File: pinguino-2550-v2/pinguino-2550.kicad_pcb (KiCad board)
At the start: 2 copper layers, 100 x 50 mm, 28 parts, among them J1 USB, J10 D1, J11 D2, J12 D3, J2 BATT, J3 SELECT, J4 A0, J5 A1, J6 PWM-1, J8 UART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

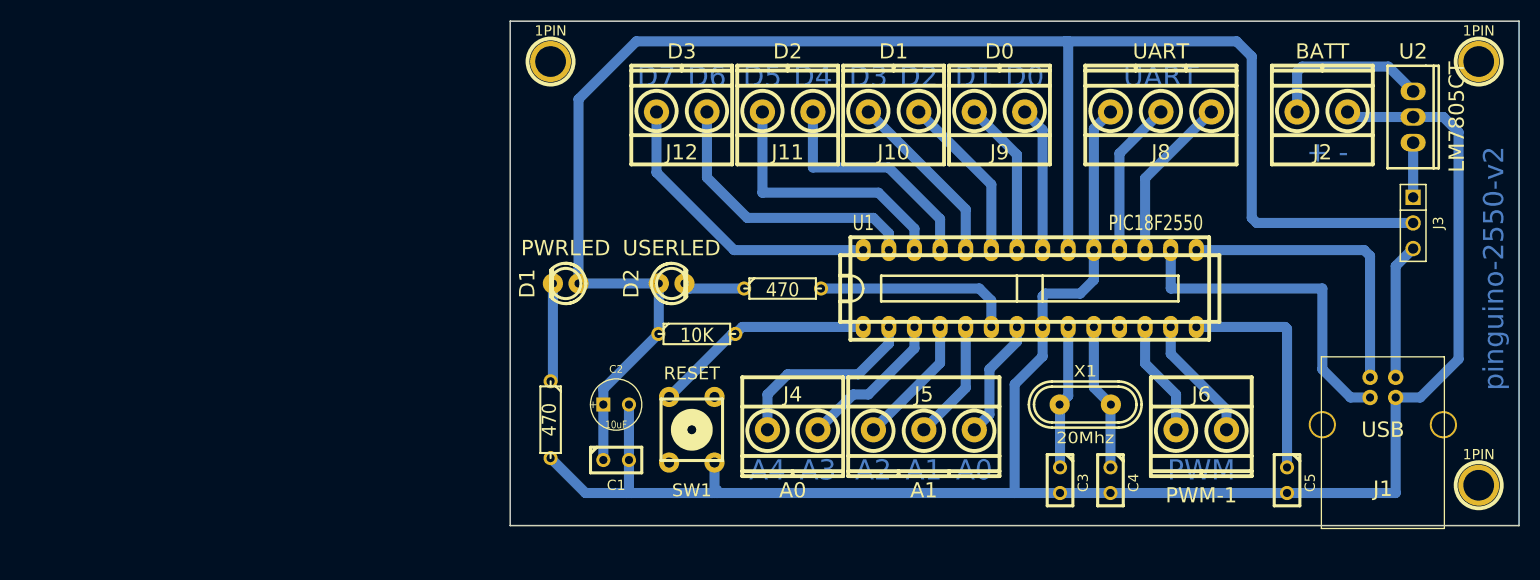
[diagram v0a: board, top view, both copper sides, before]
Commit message: Added BoM. Fixed pcbnew paper size.
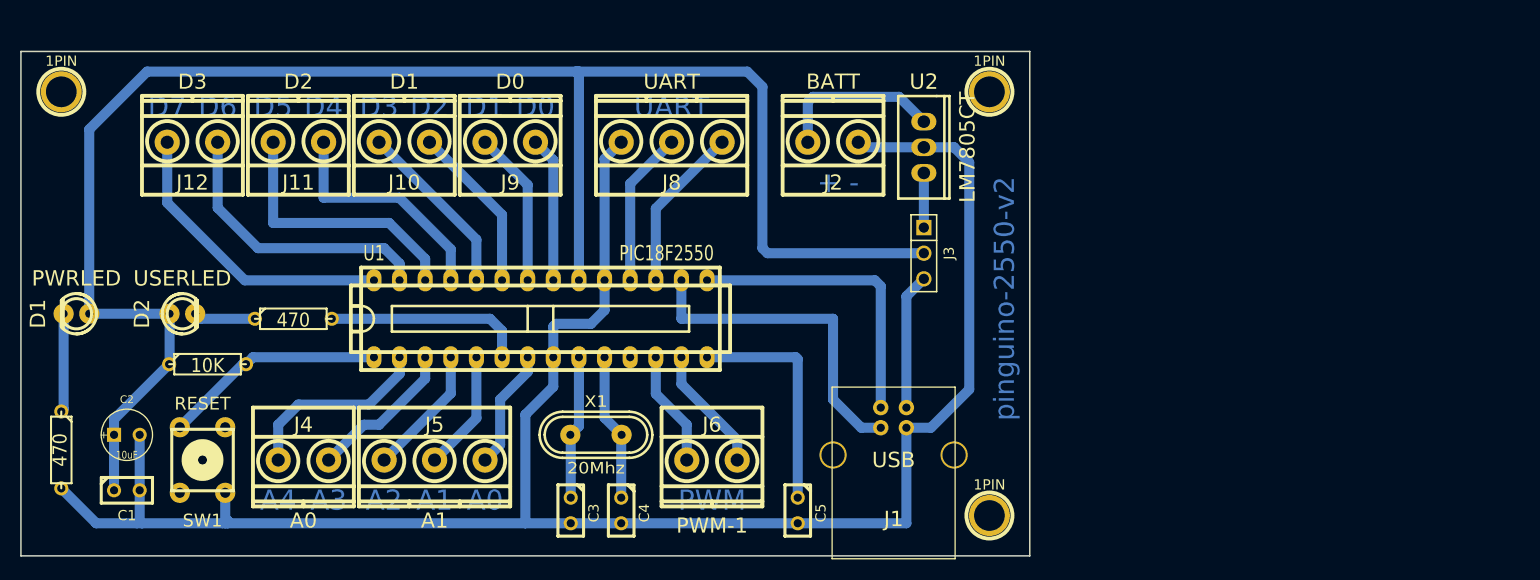
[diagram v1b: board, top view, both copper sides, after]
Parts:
- moved 1PIN 48.6 mm to (147.5, 90.0)
- moved 1PIN 48.6 mm to (147.5, 48.0)
- moved 1PIN 48.6 mm to (55.5, 48.0)
- moved C1 48.6 mm to (62.0, 87.5)
- moved C2 48.6 mm to (62.0, 82.0)
- moved C3 48.6 mm to (106.0, 89.5)
- moved C4 48.6 mm to (111.0, 89.5)
- moved C5 48.6 mm to (128.5, 89.5)
- moved D1 48.6 mm to (57.0, 70.0)
- moved D2 48.6 mm to (67.5, 70.0)
- moved J1 48.6 mm to (138.0, 84.0)
- moved J10 48.6 mm to (89.5, 53.0)
- moved J11 48.6 mm to (79.0, 53.0)
- moved J12 48.6 mm to (68.5, 53.0)
- moved J2 48.6 mm to (132.0, 53.0)
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
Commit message: Cupper layer text mirroring.
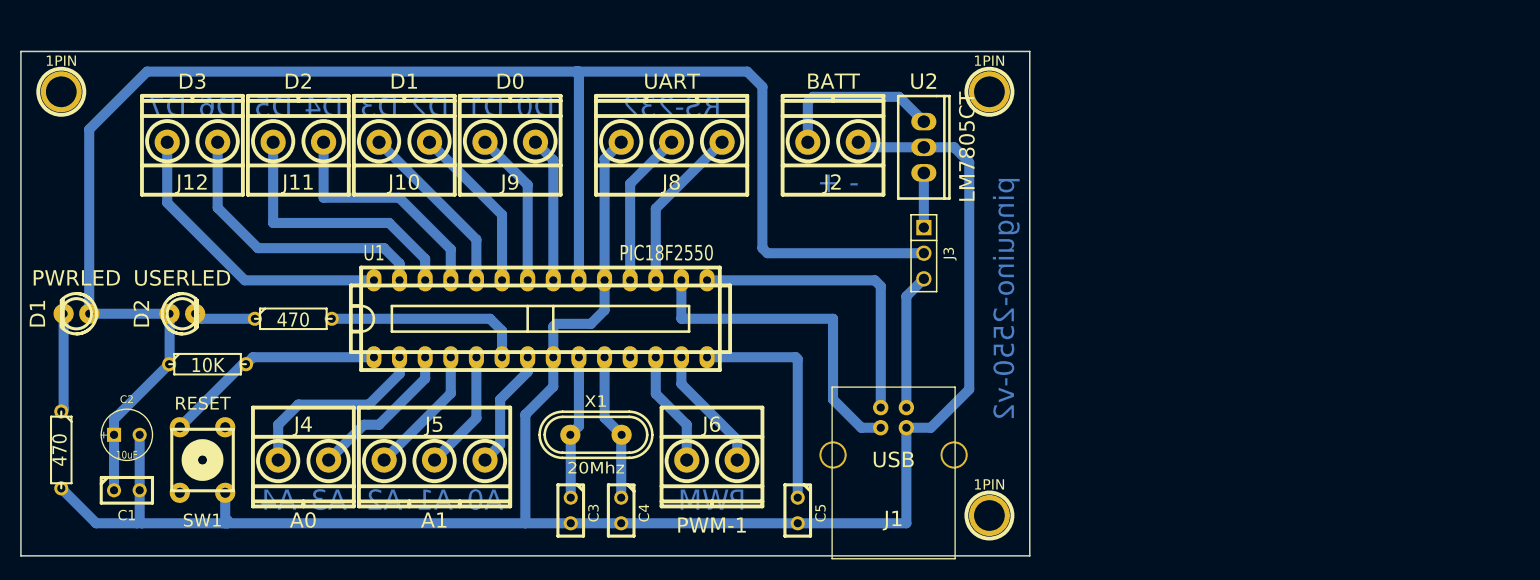
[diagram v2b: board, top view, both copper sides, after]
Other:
- board text added: "RS-232"
- board text removed: "UART"
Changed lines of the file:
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@@
     (links 50)
     (no_connects 0)
-    (area 23.85 31.925001 214.577381 413.25)
+    (area 13.35 34.925001 166.077381 283.35)
     (thickness 1.6)
     (drawings 24)
@@
     (nets 32)
   )
-  (page User 210.007 297.002 portrait)
+  (page User 431.8 279.4 portrait)
   (title_block
     (title "Pinguino 2550")
@@
     (19 F.Paste user hide)
     (20 B.SilkS user hide)
-    (21 F.SilkS user hide)
+    (21 F.SilkS user)
     (22 B.Mask user hide)
     (23 F.Mask user hide)
@@
   )
   (gr_text A4 (at 77 88.5) (layer B.Cu)
-    (effects (font (size 2 2) (thickness 0.3)))
+    (effects (font (size 2 2) (thickness 0.3)) (justify mirror))
   )
   (gr_text A3 (at 82 88.5) (layer B.Cu)
-    (effects (font (size 2 2) (thickness 0.3)))
+    (effects (font (size 2 2) (thickness 0.3)) (justify mirror))
   )
   (gr_text A2 (at 87.5 88.5) (layer B.Cu)
-    (effects (font (size 2 2) (thickness 0.3)))
+    (effects (font (size 2 2) (thickness 0.3)) (justify mirror))
   )
   (gr_text A1 (at 92.5 88.5) (layer B.Cu)
-    (effects (font (size 2 2) (thickness 0.3)))
+    (effects (font (size 2 2) (thickness 0.3)) (justify mirror))
   )
   (gr_text A0 (at 97.5 88.5) (layer B.Cu)
-    (effects (font (size 2 2) (thickness 0.3)))
+    (effects (font (size 2 2) (thickness 0.3)) (justify mirror))
   )
   (gr_text PWM (at 120 88.5) (layer B.Cu)
-    (effects (font (size 2 2) (thickness 0.3)))
+    (effects (font (size 2 2) (thickness 0.3)) (justify mirror))
   )
   (gr_text D7 (at 66 49.5) (layer B.Cu)
-    (effects (font (size 2 2) (thickness 0.3)))
+    (effects (font (size 2 2) (thickness 0.3)) (justify mirror))
   )
   (gr_text D6 (at 71 49.5) (layer B.Cu)
-    (effects (font (size 2 2) (thickness 0.3)))
+    (effects (font (size 2 2) (thickness 0.3)) (justify mirror))
   )
   (gr_text D5 (at 76.5 49.5) (layer B.Cu)
-    (effects (font (size 2 2) (thickness 0.3)))
+    (effects (font (size 2 2) (thickness 0.3)) (justify mirror))
   )
   (gr_text D4 (at 81.5 49.5) (layer B.Cu)
-    (effects (font (size 2 2) (thickness 0.3)))
+    (effects (font (size 2 2) (thickness 0.3)) (justify mirror))
   )
   (gr_text D3 (at 87 49.5) (layer B.Cu)
-    (effects (font (size 2 2) (thickness 0.3)))
+    (effects (font (size 2 2) (thickness 0.3)) (justify mirror))
   )
   (gr_text D2 (at 92 49.5) (layer B.Cu)
-    (effects (font (size 2 2) (thickness 0.3)))
+    (effects (font (size 2 2) (thickness 0.3)) (justify mirror))
   )
   (gr_text D1 (at 97.5 49.5) (layer B.Cu)
-    (effects (font (size 2 2) (thickness 0.3)))
+    (effects (font (size 2 2) (thickness 0.3)) (justify mirror))
   )
   (gr_text D0 (at 102.5 49.5) (layer B.Cu)
-    (effects (font (size 2 2) (thickness 0.3)))
-  )
-  (gr_text UART (at 116 49.5) (layer B.Cu)
-    (effects (font (size 2 2) (thickness 0.3)))
+    (effects (font (size 2 2) (thickness 0.3)) (justify mirror))
+  )
+  (gr_text RS-232 (at 116 49.5) (layer B.Cu)
+    (effects (font (size 2 2) (thickness 0.3)) (justify mirror))
   )
   (gr_text "+ -" (at 132.5 57) (layer B.Cu)
@@
   )
   (gr_text pinguino-2550-v2 (at 149 68.5 90) (layer B.Cu)
-    (effects (font (size 2 2) (thickness 0.3)))
+    (effects (font (size 2 2) (thickness 0.3)) (justify mirror))
   )
   (gr_line (start 51.5 44) (end 151.5 44) (angle 90) (layer Edge.Cuts) (width 0.15))

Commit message: Fixed bornier modules text.
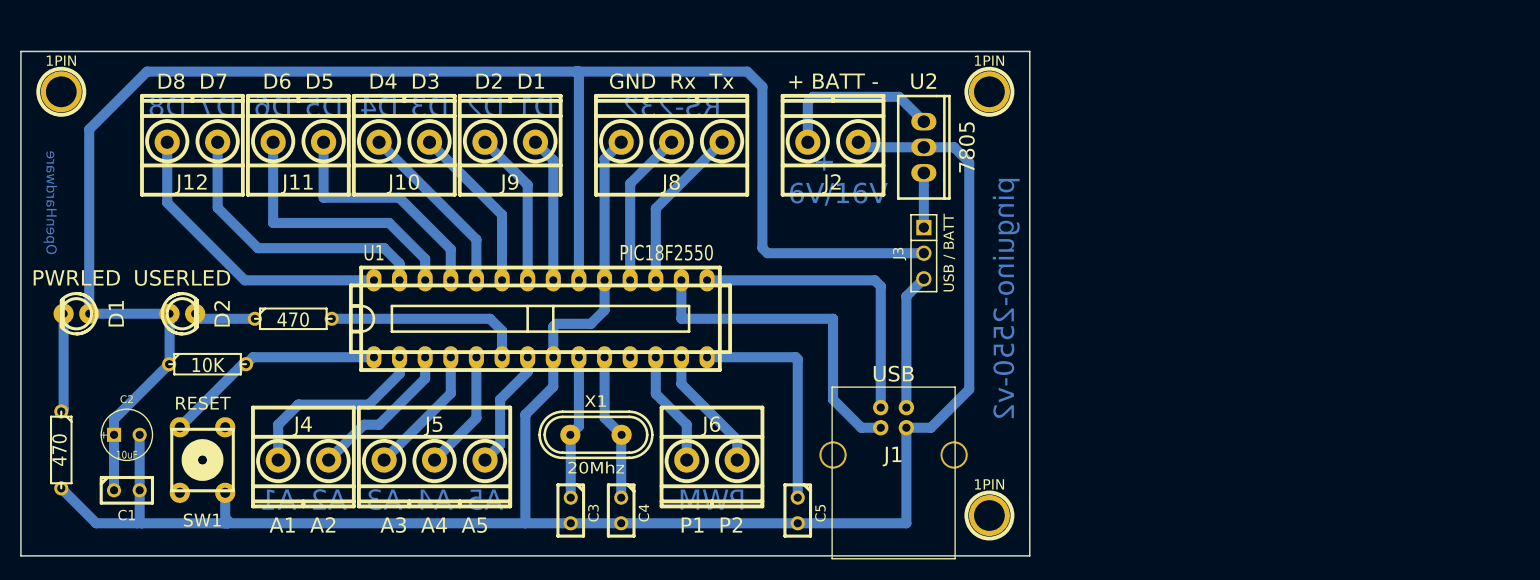
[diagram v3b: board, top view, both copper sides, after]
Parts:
- J10: value D1 -> D4 D3
- J11: value D2 -> D6 D5
- J12: value D3 -> D8 D7
- J2: value BATT -> + BATT -
- J3: value SELECT -> USB / BATT
- J4: value A0 -> A1 A2
- J5: value A1 -> A3 A4 A5
- J6: value PWM-1 -> P1 P2
- J8: value UART -> GND Rx Tx
- J9: value D0 -> D2 D1
- U2: value LM7805CT -> 7805
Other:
- board text added: "+ - 6V/16V"
- board text added: "A5"
- board text added: "D8"
- board text added: "OpenHardware"
- board text removed: "+ -"
- board text removed: "A0"
- board text removed: "D0"
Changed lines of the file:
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@@
     (area 13.35 34.925001 166.077381 283.35)
     (thickness 1.6)
-    (drawings 24)
+    (drawings 25)
     (tracks 140)
     (zones 0)
@@
     (tags USB)
     (clearance 0.1)
-    (fp_text reference J1 (at 0 6.35) (layer F.SilkS)
+    (fp_text reference J1 (at 0 0) (layer F.SilkS)
       (effects (font (size 1.524 1.524) (thickness 0.3048)))
     )
-    (fp_text value USB (at 0 0.5) (layer F.SilkS)
+    (fp_text value USB (at 0 -8) (layer F.SilkS)
       (effects (font (size 1.524 1.524) (thickness 0.3048)))
     )
@@
     (descr "Connecteur 3 pins")
     (tags "CONN DEV")
-    (fp_text reference J3 (at 0 -2.5 270) (layer F.SilkS)
+    (fp_text reference J3 (at 0 2.5 270) (layer F.SilkS)
       (effects (font (size 1.016 1.016) (thickness 0.1524)))
     )
-    (fp_text value SELECT (at 0 -2.159 270) (layer F.SilkS) hide
+    (fp_text value "USB / BATT" (at 0 -2.5 270) (layer F.SilkS)
       (effects (font (size 1.016 1.016) (thickness 0.1524)))
     )
@@
       (effects (font (size 1.524 1.524) (thickness 0.3048)))
     )
-    (fp_text value LM7805CT (at 0 -4.318 270) (layer F.SilkS)
+    (fp_text value 7805 (at 0 -4.318 270) (layer F.SilkS)
       (effects (font (size 1.524 1.524) (thickness 0.3048)))
     )
@@
       (effects (font (size 1.5 1.5) (thickness 0.3)))
     )
-    (fp_text value D0 (at 0 6 180) (layer F.SilkS)
+    (fp_text value "D2  D1" (at 0 6 180) (layer F.SilkS)
       (effects (font (size 1.5 1.5) (thickness 0.3)))
     )
@@
       (effects (font (size 1.5 1.5) (thickness 0.3)))
     )
-    (fp_text value D1 (at 0 6 180) (layer F.SilkS)
+    (fp_text value "D4  D3" (at 0 6 180) (layer F.SilkS)
       (effects (font (size 1.5 1.5) (thickness 0.3)))
     )
@@
       (effects (font (size 1.5 1.5) (thickness 0.3)))
     )
-    (fp_text value D2 (at 0 6 180) (layer F.SilkS)
+    (fp_text value "D6  D5" (at 0 6 180) (layer F.SilkS)
       (effects (font (size 1.5 1.5) (thickness 0.3)))
     )
@@
       (effects (font (size 1.5 1.5) (thickness 0.3)))
     )
-    (fp_text value D3 (at 0 6 180) (layer F.SilkS)
+    (fp_text value "D8  D7" (at 0 6 180) (layer F.SilkS)
       (effects (font (size 1.5 1.5) (thickness 0.3)))
     )
@@
       (effects (font (size 1.5 1.5) (thickness 0.3)))
     )
-    (fp_text value A1 (at 0 6) (layer F.SilkS)
+    (fp_text value "A3  A4  A5" (at 0 6.5) (layer F.SilkS)
       (effects (font (size 1.5 1.5) (thickness 0.3)))
     )
@@
       (effects (font (size 1.5 1.5) (thickness 0.3)))
     )
-    (fp_text value A0 (at 0 6) (layer F.SilkS)
+    (fp_text value "A1  A2" (at 0 6.5) (layer F.SilkS)
       (effects (font (size 1.5 1.5) (thickness 0.3)))
     )
@@
       (effects (font (size 1.5 1.5) (thickness 0.3)))
     )
-    (fp_text value UART (at 0 6 180) (layer F.SilkS)
+    (fp_text value "GND  Rx  Tx" (at 0 6 180) (layer F.SilkS)
       (effects (font (size 1.5 1.5) (thickness 0.3)))
     )
@@
       (effects (font (size 1.5 1.5) (thickness 0.3)))
     )
-    (fp_text value PWM-1 (at 0 6.5) (layer F.SilkS)
+    (fp_text value "P1  P2" (at 0 6.5) (layer F.SilkS)
       (effects (font (size 1.5 1.5) (thickness 0.3)))
     )
@@
     (tags led)
     (clearance 0.2)
-    (fp_text reference D1 (at 0 3.81 270) (layer F.SilkS)
+    (fp_text reference D1 (at 0 -4 270) (layer F.SilkS)
       (effects (font (size 1.524 1.524) (thickness 0.3048)))
     )
@@
     (tags led)
     (clearance 0.2)
-    (fp_text reference D2 (at 0 -4 90) (layer F.SilkS)
+    (fp_text reference D2 (at 0 4 90) (layer F.SilkS)
       (effects (font (size 1.524 1.524) (thickness 0.3048)))
     )
@@
       (effects (font (size 1.5 1.5) (thickness 0.3)))
     )
-    (fp_text value BATT (at 0 6 180) (layer F.SilkS)
+    (fp_text value "+ BATT -" (at 0 6 180) (layer F.SilkS)
       (effects (font (size 1.5 1.5) (thickness 0.3)))
     )
@@
     )
   )
+  (gr_text OpenHardware (at 54.5 59 270) (layer B.Cu)
+    (effects (font (size 1 1) (thickness 0.25)) (justify mirror))
+  )
   (gr_text "Referencias\n=======\n\nUSB: Conector USB.\nBATT: Conector alimentación externa.\nJ3: Selector alimentación externa o USB.\nD0: Salidas digitales 0 y 1.\nD1: Salidas digitales 2 y 3.\nD2: Salidas digitales 4 y 5.\nD3: Salidas digitales 6 y 7.\nPWM: Salidas analógicas 0 y 1.\nA1: Entradas analógicas 0, 1 y 2.\nA0: Entradas analógicas 3 y 4.\nSW1: Interruptor reset." (at 13.5 241.5) (layer Cmts.User)
     (effects (font (size 2 2) (thickness 0.3)) (justify left))
@@
     (arrow2b (pts (xy 51.5 37.000001) (xy 52.626503 36.413581)))
   )
-  (gr_text A4 (at 77 88.5) (layer B.Cu)
-    (effects (font (size 2 2) (thickness 0.3)) (justify mirror))
-  )
-  (gr_text A3 (at 82 88.5) (layer B.Cu)
-    (effects (font (size 2 2) (thickness 0.3)) (justify mirror))
-  )
-  (gr_text A2 (at 87.5 88.5) (layer B.Cu)
-    (effects (font (size 2 2) (thickness 0.3)) (justify mirror))
-  )
-  (gr_text A1 (at 92.5 88.5) (layer B.Cu)
-    (effects (font (size 2 2) (thickness 0.3)) (justify mirror))
-  )
-  (gr_text A0 (at 97.5 88.5) (layer B.Cu)
+  (gr_text A1 (at 77 88.5) (layer B.Cu)
+    (effects (font (size 2 2) (thickness 0.3)) (justify mirror))
+  )
+  (gr_text A2 (at 82 88.5) (layer B.Cu)
+    (effects (font (size 2 2) (thickness 0.3)) (justify mirror))
+  )
+  (gr_text A3 (at 87.5 88.5) (layer B.Cu)
+    (effects (font (size 2 2) (thickness 0.3)) (justify mirror))
+  )
+  (gr_text A4 (at 92.5 88.5) (layer B.Cu)
+    (effects (font (size 2 2) (thickness 0.3)) (justify mirror))
+  )
+  (gr_text A5 (at 97.5 88.5) (layer B.Cu)
     (effects (font (size 2 2) (thickness 0.3)) (justify mirror))
   )
@@
     (effects (font (size 2 2) (thickness 0.3)) (justify mirror))
   )
-  (gr_text D7 (at 66 49.5) (layer B.Cu)
-    (effects (font (size 2 2) (thickness 0.3)) (justify mirror))
-  )
-  (gr_text D6 (at 71 49.5) (layer B.Cu)
-    (effects (font (size 2 2) (thickness 0.3)) (justify mirror))
-  )
-  (gr_text D5 (at 76.5 49.5) (layer B.Cu)
-    (effects (font (size 2 2) (thickness 0.3)) (justify mirror))
-  )
-  (gr_text D4 (at 81.5 49.5) (layer B.Cu)
-    (effects (font (size 2 2) (thickness 0.3)) (justify mirror))
-  )
-  (gr_text D3 (at 87 49.5) (layer B.Cu)
-    (effects (font (size 2 2) (thickness 0.3)) (justify mirror))
-  )
-  (gr_text D2 (at 92 49.5) (layer B.Cu)
-    (effects (font (size 2 2) (thickness 0.3)) (justify mirror))
-  )
-  (gr_text D1 (at 97.5 49.5) (layer B.Cu)
-    (effects (font (size 2 2) (thickness 0.3)) (justify mirror))
-  )
-  (gr_text D0 (at 102.5 49.5) (layer B.Cu)
+  (gr_text D8 (at 66 49.5) (layer B.Cu)
+    (effects (font (size 2 2) (thickness 0.3)) (justify mirror))
+  )
+  (gr_text D7 (at 71 49.5) (layer B.Cu)
+    (effects (font (size 2 2) (thickness 0.3)) (justify mirror))
+  )
+  (gr_text D6 (at 76.5 49.5) (layer B.Cu)
+    (effects (font (size 2 2) (thickness 0.3)) (justify mirror))
+  )
+  (gr_text D5 (at 81.5 49.5) (layer B.Cu)
+    (effects (font (size 2 2) (thickness 0.3)) (justify mirror))
+  )
+  (gr_text D4 (at 87 49.5) (layer B.Cu)
+    (effects (font (size 2 2) (thickness 0.3)) (justify mirror))
+  )
+  (gr_text D3 (at 92 49.5) (layer B.Cu)
+    (effects (font (size 2 2) (thickness 0.3)) (justify mirror))
+  )
+  (gr_text D2 (at 97.5 49.5) (layer B.Cu)
+    (effects (font (size 2 2) (thickness 0.3)) (justify mirror))
+  )
+  (gr_text D1 (at 102.5 49.5) (layer B.Cu)
     (effects (font (size 2 2) (thickness 0.3)) (justify mirror))
   )
@@
     (effects (font (size 2 2) (thickness 0.3)) (justify mirror))
   )
-  (gr_text "+ -" (at 132.5 57) (layer B.Cu)
+  (gr_text "+  -\n6V/16V" (at 132.5 56.5) (layer B.Cu)
     (effects (font (size 2 2) (thickness 0.3)))
   )
